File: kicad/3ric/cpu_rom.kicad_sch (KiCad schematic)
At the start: 15 parts, among them J1_AND 74LS08, J3_DEV_DECODE 74LS154, K1_CPU 6502-library_65C02S-2, K2_ROM SST39SF040

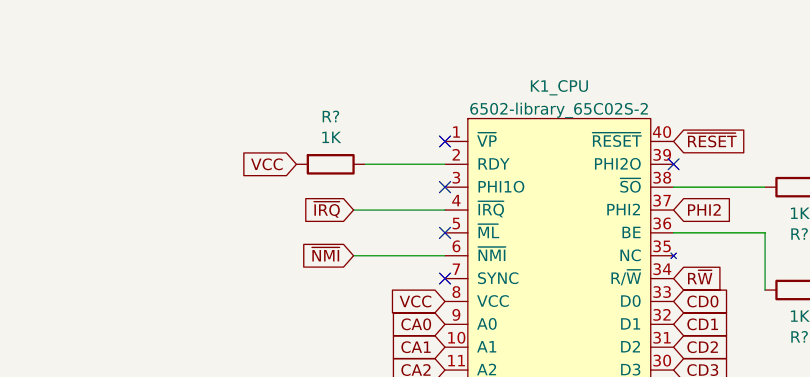
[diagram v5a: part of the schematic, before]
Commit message: completed?  Everything wired in layout creator and first draft of completed schematic
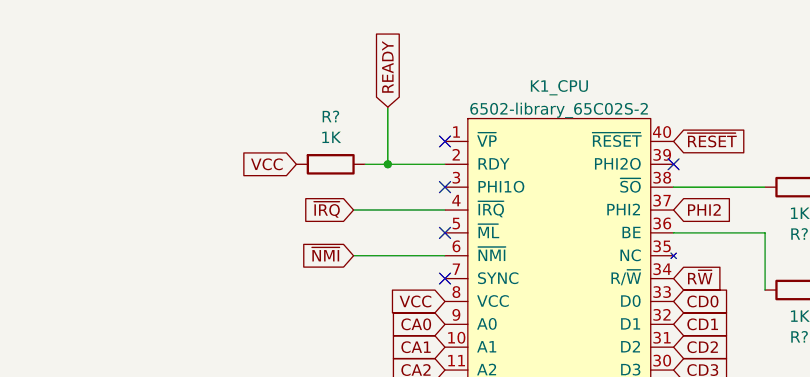
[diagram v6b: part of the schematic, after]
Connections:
- net READY: now reaches K1_CPU.2 (RDY), R?.1
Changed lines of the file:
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@@
+	)
+	(junction
+		(at 118.11 44.45)
+		(diameter 0)
+		(color 0 0 0 0)
 	)
 	(junction
@@
 	(wire
 		(pts
+			(xy 118.11 44.45) (xy 124.46 44.45)
+		)
+		(stroke
+			(width 0)
+			(type default)
+		)
+	)
+	(wire
+		(pts
 			(xy 200.66 100.33) (xy 232.41 100.33)
 		)
@@
 	(wire
 		(pts
-			(xy 115.57 44.45) (xy 124.46 44.45)
+			(xy 118.11 38.1) (xy 118.11 44.45)
+		)
+		(stroke
+			(width 0)
+			(type default)
+		)
+	)
+	(wire
+		(pts
+			(xy 115.57 44.45) (xy 118.11 44.45)
 		)
 		(stroke
@@
 				(hide yes)
 			)
+		)
+	)
+	(global_label "READY"
+		(shape input)
+		(at 118.11 38.1 90)
+		(fields_autoplaced yes)
+		(effects
+			(font
+				(size 1.27 1.27)
+			)
+			(justify left)
+		)
+		(property "Intersheetrefs" "${INTERSHEET_REFS}"
+			(at 118.11 29.2486 90)
+			(effects
+				(font
+					(size 1.27 1.27)
+				)
+				(justify left)
+				(hide yes)
+			)

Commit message: cleaning up of the schematic
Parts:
- removed A4_AND, J1_AND: 74LS08, symbol 74xx:74LS08
- removed R? (x6): 1K, Resistor_THT:R_Axial_DIN0207_L6.3mm_D2.5mm_P7.62mm_Horizontal, symbol Device:R
- removed Z1_IRQ_AND: 74LS11, symbol 74xx:74LS11
- added J1_AND1: 74LS08, Package_DIP:DIP-14_W7.62mm_Socket, symbol 74xx:74LS08
- added R26, R27, R28, R29, R30, R31: 1K, Resistor_THT:R_Axial_DIN0207_L6.3mm_D2.5mm_P7.62mm_Horizontal, symbol Device:R
- gave numbers to parts that had none: 3
- renumbered J3_DEV_DECODE to J3_DEV_DECODE1, K1_CPU to K1_CPU1, K2_ROM to K2_ROM1
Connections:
- net GND: no longer K2_ROM1.1 (A18), K2_ROM1.30 (A17)
- net VCC: now also R26.2, R27.2, R28.2, R29.2, R30.2, R31.2
- net ~{IRQEXT}: now also J1_AND1.13, R31.1
- net ~{IRQ_ACIA}: now also J1_AND1.1, R26.1
- net ~{IRQ_MB1}: now also J1_AND1.9, R30.1
- net ~{IRQ_MB2}: now also J1_AND1.10, R29.1
- net ~{IRQ_VIA1}: now also J1_AND1.2, R27.1
- net ~{IRQ}: now also J1_AND1.11
- net ~{NMIEXT}: now also J1_AND1.5, R28.1
- net ~{NMI}: now also J1_AND1.6
- net C0XX: no longer names the net of J3_DEV_DECODE1.1 (S0)
- new net: J1_AND1.3, J1_AND1.4
- new net: J1_AND1.12, J1_AND1.8
- new net ROM1: K2_ROM1.1 (A18)
- new net ROM2: K2_ROM1.30 (A17)
- no-connect marks 13 -> 14

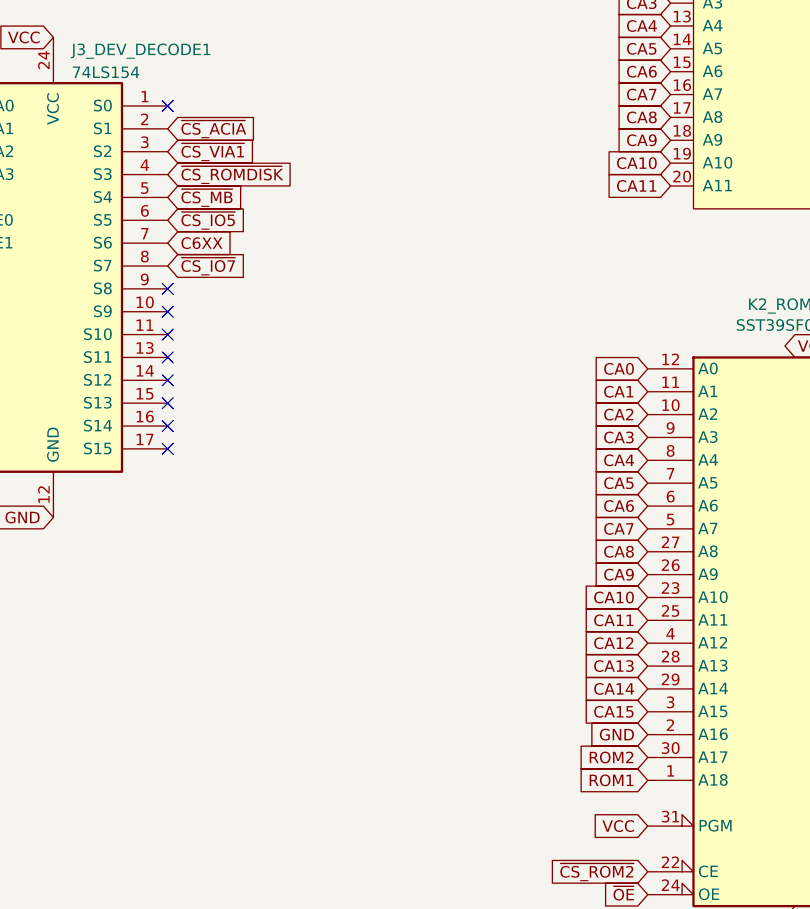
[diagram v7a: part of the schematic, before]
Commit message: updated schematics and PCB PNG of the breadboard layout
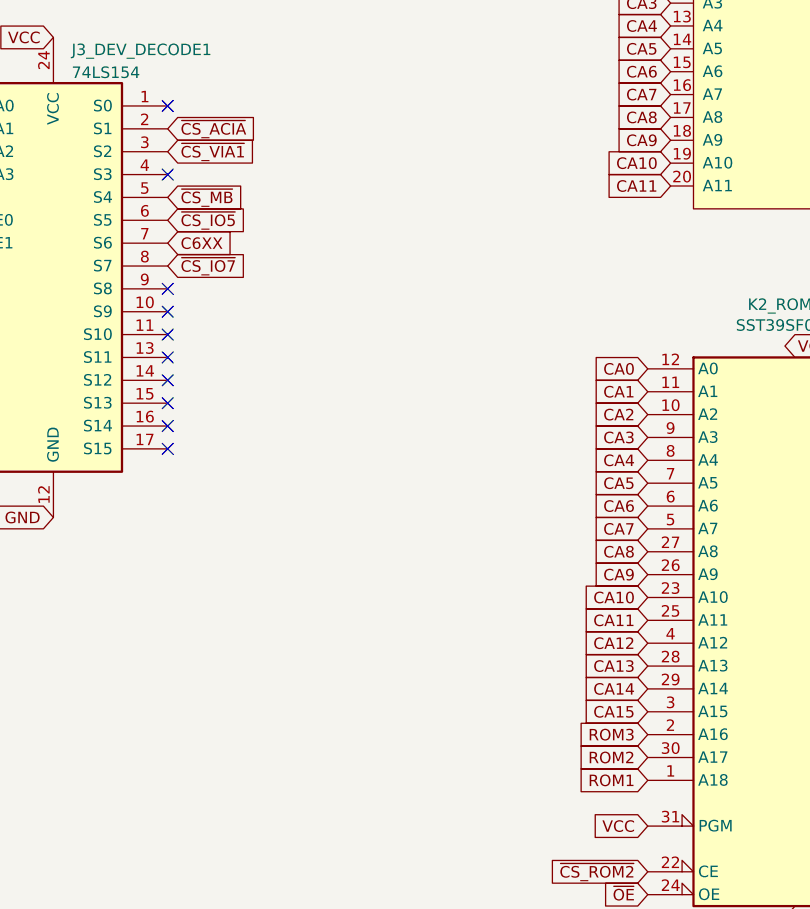
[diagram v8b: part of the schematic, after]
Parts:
- R26, R27, R28, R29, R30, R31: footprint Resistor_THT:R_Axial_DIN0207_L6.3mm_D2.5mm_P7.62mm_Horizontal -> Resistor_SMD:R_0805_2012Metric_Pad1.20x1.40mm_HandSolder
- R4, R5, R6: footprint Resistor_THT:R_Axial_DIN0207_L6.3mm_D2.5mm_P7.62mm_Horizontal -> Resistor_SMD:R_0402_1005Metric_Pad0.72x0.64mm_HandSolder
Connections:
- net GND: no longer K2_ROM1.2 (A16)
- net ~{CS_ROMDISK}: no longer names the net of J3_DEV_DECODE1.4 (S3)
- new net ROM3: K2_ROM1.2 (A16)
- no-connect marks 14 -> 15
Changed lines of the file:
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@@
 	)
 	(no_connect
+		(at 68.58 88.9)
+	)
+	(no_connect
 		(at 68.58 114.3)
 	)
@@
 		)
 	)
-	(global_label "~{CS_ROMDISK}"
-		(shape input)
-		(at 68.58 88.9 0)
-		(fields_autoplaced yes)
-		(effects
-			(font
-				(size 1.27 1.27)
-			)
-			(justify left)
-		)
-		(property "Intersheetrefs" "${INTERSHEET_REFS}"
-			(at -154.94 36.83 0)
-			(effects
-				(font
-					(size 1.27 1.27)
-				)
-				(hide yes)
-			)
-		)
-	)
 	(global_label "CD0"
 		(shape input)
@@
 		)
 	)
-	(global_label "GND"
-		(shape input)
-		(at 121.92 151.13 180)
-		(fields_autoplaced yes)
-		(effects
-			(font
-				(size 1.27 1.27)
-			)
-			(justify right)
-		)
-		(property "Intersheetrefs" "${INTERSHEET_REFS}"
-			(at 165.1 193.04 0)
-			(effects
-				(font
-					(size 1.27 1.27)
-				)
-				(hide yes)
-			)
-		)
-	)
 	(global_label "CD4"
 		(shape input)
@@
 		)
 	)
+	(global_label "ROM3"
+		(shape input)
+		(at 121.92 151.13 180)
+		(fields_autoplaced yes)
+		(effects
+			(font
+				(size 1.27 1.27)
+			)
+			(justify right)
+		)
+		(property "Intersheetrefs" "${INTERSHEET_REFS}"
+			(at 113.6734 151.13 0)
+			(effects
+				(font
+					(size 1.27 1.27)
+				)
+				(justify right)
+				(hide yes)
+			)
+		)
+	)
 	(global_label "VCC"
 		(shape input)
@@
 			)
 		)
-		(property "Footprint" "Resistor_THT:R_Axial_DIN0207_L6.3mm_D2.5mm_P7.62mm_Horizontal"
+		(property "Footprint" "Resistor_SMD:R_0805_2012Metric_Pad1.20x1.40mm_HandSolder"
 			(at 240.03 137.922 90)
 			(effects
@@
 			)
 		)
-		(property "Footprint" "Resistor_THT:R_Axial_DIN0207_L6.3mm_D2.5mm_P7.62mm_Horizontal"
+		(property "Footprint" "Resistor_SMD:R_0805_2012Metric_Pad1.20x1.40mm_HandSolder"
 			(at 217.17 50.292 90)
 			(effects
@@
 			)
 		)
-		(property "Footprint" "Resistor_THT:R_Axial_DIN0207_L6.3mm_D2.5mm_P7.62mm_Horizontal"
+		(property "Footprint" "Resistor_SMD:R_0402_1005Metric_Pad0.72x0.64mm_HandSolder"
 			(at 111.76 42.672 90)
 			(effects
@@
 			)
 		)
-		(property "Footprint" "Resistor_THT:R_Axial_DIN0207_L6.3mm_D2.5mm_P7.62mm_Horizontal"
+		(property "Footprint" "Resistor_SMD:R_0805_2012Metric_Pad1.20x1.40mm_HandSolder"
 			(at 218.44 104.902 90)
 			(effects
@@
 			)
 		)
-		(property "Footprint" "Resistor_THT:R_Axial_DIN0207_L6.3mm_D2.5mm_P7.62mm_Horizontal"
+		(property "Footprint" "Resistor_SMD:R_0805_2012Metric_Pad1.20x1.40mm_HandSolder"
 			(at 201.93 111.252 90)
 			(effects
@@
 			)
 		)
-		(property "Footprint" "Resistor_THT:R_Axial_DIN0207_L6.3mm_D2.5mm_P7.62mm_Horizontal"
+		(property "Footprint" "Resistor_SMD:R_0402_1005Metric_Pad0.72x0.64mm_HandSolder"
 			(at 163.83 60.198 90)
 			(effects
@@
 			)
 		)
-		(property "Footprint" "Resistor_THT:R_Axial_DIN0207_L6.3mm_D2.5mm_P7.62mm_Horizontal"
+		(property "Footprint" "Resistor_SMD:R_0402_1005Metric_Pad0.72x0.64mm_HandSolder"
 			(at 163.83 48.768 90)
 			(effects
@@
 			)
 		)
-		(property "Footprint" "Resistor_THT:R_Axial_DIN0207_L6.3mm_D2.5mm_P7.62mm_Horizontal"
+		(property "Footprint" "Resistor_SMD:R_0805_2012Metric_Pad1.20x1.40mm_HandSolder"
 			(at 200.66 54.102 90)
 			(effects
@@
 			)
 		)
-		(property "Footprint" "Resistor_THT:R_Axial_DIN0207_L6.3mm_D2.5mm_P7.62mm_Horizontal"
+		(property "Footprint" "Resistor_SMD:R_0805_2012Metric_Pad1.20x1.40mm_HandSolder"
 			(at 236.22 82.042 90)
 			(effects
